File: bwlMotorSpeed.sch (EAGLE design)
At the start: 8 parts, among them M1 McMaster-Carr 59835K61, Q1 IRLB8721

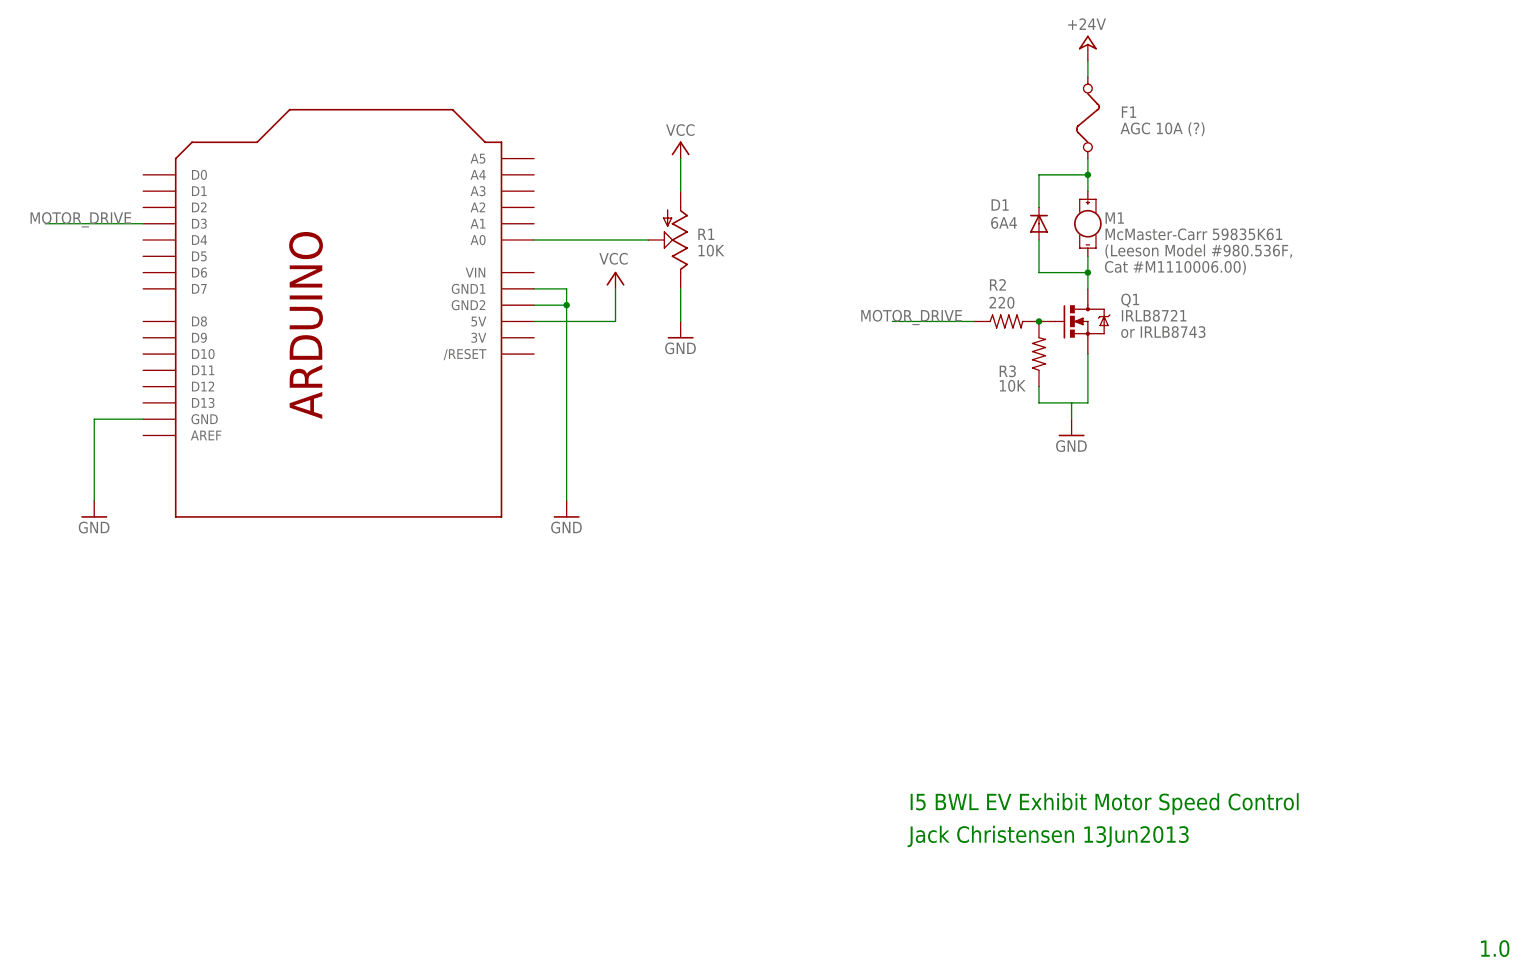
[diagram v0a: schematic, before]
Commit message: Added mode button, LED state indicators.
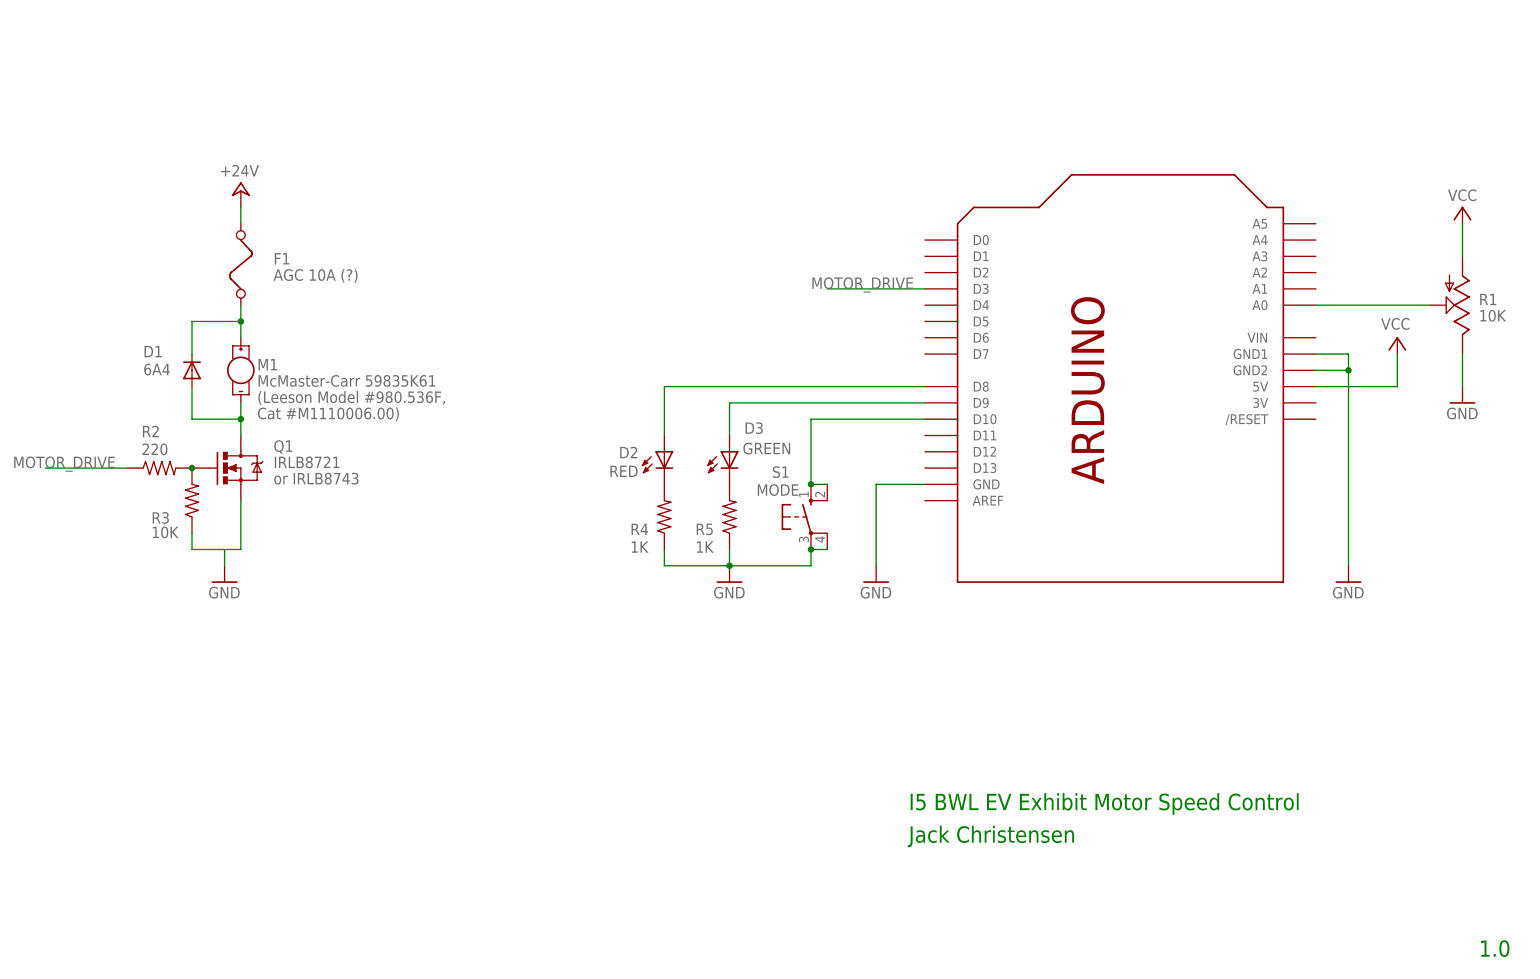
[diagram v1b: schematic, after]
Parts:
- added D2: RED, _jc:LEDCHIPLED_1206
- added D3: GREEN, _jc:LEDCHIPLED_1206
- added R4, R5: 1K, _jc:R-US_M0805
- added S1: MODE, _jc:10-XXOCT
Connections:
- new net N$3: D2.C, R4.2
- new net N$5: D3.C, R5.2
- new net N$7: S1.S, S1.S1, U$1.D10
- new net N$8: D3.A, U$1.D9
- new net N$9: D2.A, U$1.D8
- net GND: now also R4.1, R5.1, S1.P, S1.P1
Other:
- note added: "Jack Christensen"
- note removed: "Jack Christensen 13Jun2013"
- moved on the sheet: D1, F1, M1, Q1, R1, R2, R3
